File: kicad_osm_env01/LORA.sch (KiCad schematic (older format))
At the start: 15 parts, among them U5 ERIC-LORA, U6 RAK4270

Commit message: schematics awaiting review
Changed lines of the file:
@@
 AR Path="/60880AD8/608A2EE5" Ref="#PWR048"  Part="1"
 F 0 "#PWR048" H 2400 4175 50  0001 C CNN
-F 1 "+3V3" H 2415 4498 50  0000 C CNN
+F 1 "+3V3" V 2400 4550 50  0000 C CNN
 F 2 "" H 2400 4325 50  0001 C CNN
 F 3 "" H 2400 4325 50  0001 C CNN
@@
 U 1 1 6075834F
 P 8150 3800
-F 0 "U6" H 8150 4881 50  0000 C CNN
-F 1 "RAK4270" H 8150 4790 50  0000 C CNN
+F 0 "U6" H 8650 4775 50  0000 C CNN
+F 1 "RAK4270" H 8775 4675 50  0000 C CNN
 F 2 "Devtank_PCB_lib:RAK4270" H 7900 4175 50  0001 C CNN
 F 3 "" H 7900 4175 50  0001 C CNN

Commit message: rough layout with throwdown of parts
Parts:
- C70: footprint Capacitor_SMD:C_0603_1608Metric -> Capacitor_SMD:C_0402_1005Metric
- TP30, TP31, TP32, TP33, TP34, TP35: footprint TestPoint:TestPoint_THTPad_D1.0mm_Drill0.5mm -> TestPoint:TestPoint_Pad_D1.5mm
- U6: footprint Devtank_PCB_lib:RAK4270 -> Devtank_PCB_lib:RAK4270_WisDuo_LPWAN_Module
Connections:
- net LORA_RX: now also U6.1 (UART2_RX); no longer U6.5 (UART1_RX)
- net LORA_TX: now also U6.2 (UART2_TX); no longer U6.4 (UART1_TX)
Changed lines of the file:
@@
 $Descr A4 11693 8268
 encoding utf-8
-Sheet 3 11
+Sheet 3 9
 Title ""
 Date ""
@@
 F 0 "TP31" V 2950 3700 50  0000 C CNN
 F 1 "Test_Point" V 2950 3800 50  0001 C CNN
-F 2 "TestPoint:TestPoint_THTPad_D1.0mm_Drill0.5mm" H 3150 3425 50  0001 C CNN
+F 2 "TestPoint:TestPoint_Pad_D1.5mm" H 3150 3425 50  0001 C CNN
 F 3 "~" H 3150 3425 50  0001 C CNN
 	1    2950 3425
@@
 F 0 "TP32" V 2950 3925 50  0000 C CNN
 F 1 "Test_Point" V 2950 4025 50  0001 C CNN
-F 2 "TestPoint:TestPoint_THTPad_D1.0mm_Drill0.5mm" H 3150 3650 50  0001 C CNN
+F 2 "TestPoint:TestPoint_Pad_D1.5mm" H 3150 3650 50  0001 C CNN
 F 3 "~" H 3150 3650 50  0001 C CNN
 	1    2950 3650
@@
 F 0 "TP33" V 2950 4125 50  0000 C CNN
 F 1 "Test_Point" V 2950 4225 50  0001 C CNN
-F 2 "TestPoint:TestPoint_THTPad_D1.0mm_Drill0.5mm" H 3150 3850 50  0001 C CNN
+F 2 "TestPoint:TestPoint_Pad_D1.5mm" H 3150 3850 50  0001 C CNN
 F 3 "~" H 3150 3850 50  0001 C CNN
 	1    2950 3850
@@
 F 0 "TP30" V 2950 3475 50  0000 C CNN
 F 1 "Test_Point" V 2950 3575 50  0001 C CNN
-F 2 "TestPoint:TestPoint_THTPad_D1.0mm_Drill0.5mm" H 3150 3200 50  0001 C CNN
+F 2 "TestPoint:TestPoint_Pad_D1.5mm" H 3150 3200 50  0001 C CNN
 F 3 "~" H 3150 3200 50  0001 C CNN
 	1    2950 3200
@@
 F 0 "TP34" V 2950 4350 50  0000 C CNN
 F 1 "Test_Point" V 2950 4450 50  0001 C CNN
-F 2 "TestPoint:TestPoint_THTPad_D1.0mm_Drill0.5mm" H 3150 4075 50  0001 C CNN
+F 2 "TestPoint:TestPoint_Pad_D1.5mm" H 3150 4075 50  0001 C CNN
 F 3 "~" H 3150 4075 50  0001 C CNN
 	1    2950 4075
@@
 NoConn ~ 7275 4050
 NoConn ~ 7275 3925
-NoConn ~ 7275 3425
-NoConn ~ 7275 3300
-Wire Wire Line
-	7275 3675 6900 3675
-Wire Wire Line
-	7275 3800 6900 3800
-Text HLabel 6900 3800 0    50   Input ~ 0
+Wire Wire Line
+	7275 3425 6900 3425
+Wire Wire Line
+	7275 3300 6900 3300
+Text HLabel 6900 3300 0    50   Input ~ 0
 LORA_RX
-Text HLabel 6900 3675 0    50   Input ~ 0
+Text HLabel 6900 3425 0    50   Input ~ 0
 LORA_TX
 Text HLabel 3175 3350 0    50   Input ~ 0
@@
 F 0 "C70" H 9690 3571 50  0000 L CNN
 F 1 "100nF" H 9690 3480 50  0000 L CNN
-F 2 "Capacitor_SMD:C_0603_1608Metric" H 9613 3375 50  0001 C CNN
+F 2 "Capacitor_SMD:C_0402_1005Metric" H 9613 3375 50  0001 C CNN
 F 3 "" H 9575 3525 50  0001 C CNN
 	1    9575 3525
@@
 F 0 "TP35" V 9900 3675 50  0000 C CNN
 F 1 "Test_Point" V 9975 3625 50  0001 C CNN
-F 2 "TestPoint:TestPoint_THTPad_D1.0mm_Drill0.5mm" H 10100 3400 50  0001 C CNN
+F 2 "TestPoint:TestPoint_Pad_D1.5mm" H 10100 3400 50  0001 C CNN
 F 3 "~" H 10100 3400 50  0001 C CNN
 	1    9900 3400
@@
 F 0 "U6" H 8650 4775 50  0000 C CNN
 F 1 "RAK4270" H 8775 4675 50  0000 C CNN
-F 2 "Devtank_PCB_lib:RAK4270" H 7900 4175 50  0001 C CNN
+F 2 "Devtank_PCB_lib:RAK4270_WisDuo_LPWAN_Module" H 7900 4175 50  0001 C CNN
 F 3 "" H 7900 4175 50  0001 C CNN
 	1    8150 3800
 	1    0    0    -1
 $EndComp
+NoConn ~ 7275 3675
+NoConn ~ 7275 3800
 $EndSCHEMATC

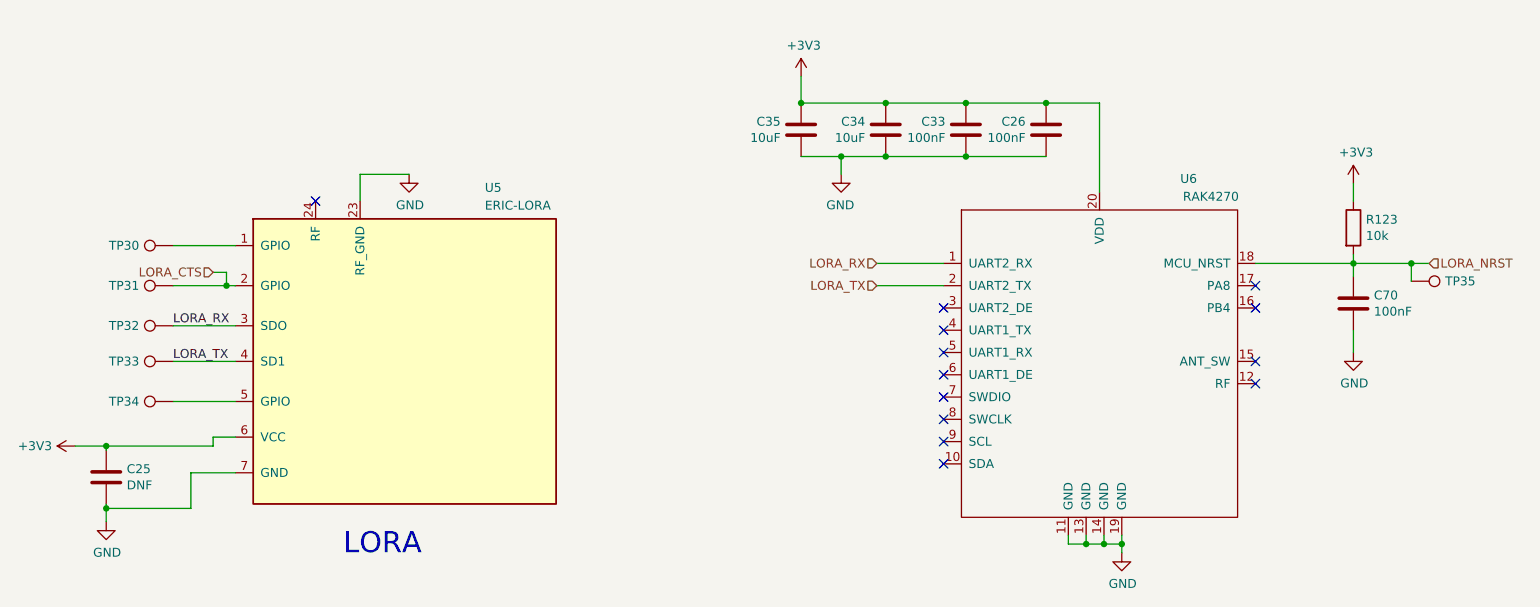
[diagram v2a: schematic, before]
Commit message: updated schematics
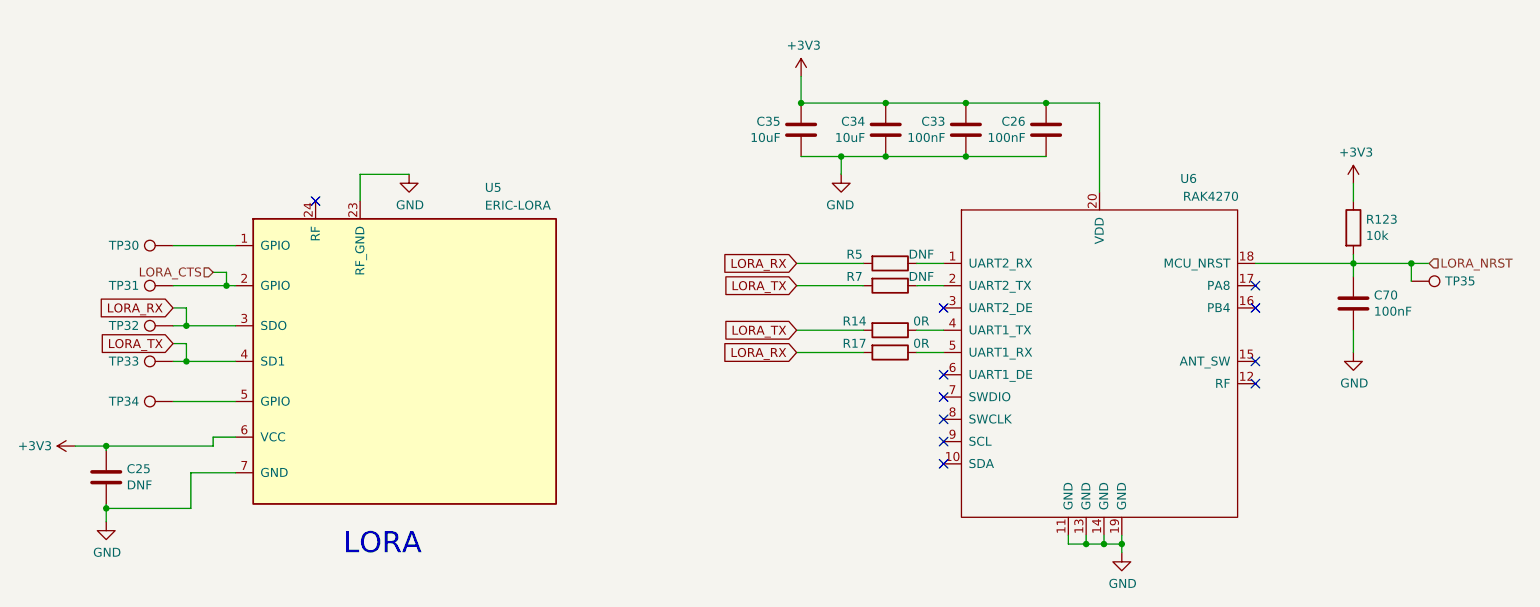
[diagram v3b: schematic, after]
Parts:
- added R14, R17: 0R, Resistor_SMD:R_0603_1608Metric, symbol device:R
- added R5, R7: DNF, Resistor_SMD:R_0603_1608Metric, symbol device:R
- C34, C35: footprint Capacitor_SMD:C_0805_2012Metric -> Capacitor_SMD:C_0402_1005Metric
- TP32, TP33: footprint TestPoint:TestPoint_Pad_D1.5mm -> TestPoint:TestPoint_THTPad_D1.0mm_Drill0.5mm
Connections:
- net LORA_RX: now also R17.2, R5.2; no longer U6.1 (UART2_RX)
- net LORA_TX: now also R14.2, R7.2; no longer U6.2 (UART2_TX)
- net at U6.4 (UART1_TX): now also R14.1
- net at U6.5 (UART1_RX): now also R17.1
- new net: R5.1, U6.1 (UART2_RX)
- new net: R7.1, U6.2 (UART2_TX)
- no-connect marks 13 -> 11
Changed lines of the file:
@@
 	3300 3425 3250 3425
 Wire Wire Line
-	3300 3650 2950 3650
-Wire Wire Line
-	3300 3850 2950 3850
-Text Label 2950 3850 0    50   ~ 0
-LORA_TX
-Text Label 2950 3650 0    50   ~ 0
-LORA_RX
+	3300 3650 3025 3650
+Wire Wire Line
+	3300 3850 3025 3850
 Wire Wire Line
 	4000 2800 4275 2800
@@
 F 0 "TP32" V 2950 3925 50  0000 C CNN
 F 1 "Test_Point" V 2950 4025 50  0001 C CNN
-F 2 "TestPoint:TestPoint_Pad_D1.5mm" H 3150 3650 50  0001 C CNN
+F 2 "TestPoint:TestPoint_THTPad_D1.0mm_Drill0.5mm" H 3150 3650 50  0001 C CNN
 F 3 "~" H 3150 3650 50  0001 C CNN
 	1    2950 3650
@@
 F 0 "TP33" V 2950 4125 50  0000 C CNN
 F 1 "Test_Point" V 2950 4225 50  0001 C CNN
-F 2 "TestPoint:TestPoint_Pad_D1.5mm" H 3150 3850 50  0001 C CNN
+F 2 "TestPoint:TestPoint_THTPad_D1.0mm_Drill0.5mm" H 3150 3850 50  0001 C CNN
 F 3 "~" H 3150 3850 50  0001 C CNN
 	1    2950 3850
@@
 F 0 "C34" H 7065 2596 50  0000 L CNN
 F 1 "10uF" H 7065 2505 50  0000 L CNN
-F 2 "Capacitor_SMD:C_0805_2012Metric" H 6988 2400 50  0001 C CNN
+F 2 "Capacitor_SMD:C_0402_1005Metric" H 6988 2400 50  0001 C CNN
 F 3 "" H 6950 2550 50  0001 C CNN
 	1    6950 2550
@@
 F 0 "C35" H 6590 2596 50  0000 L CNN
 F 1 "10uF" H 6590 2505 50  0000 L CNN
-F 2 "Capacitor_SMD:C_0805_2012Metric" H 6513 2400 50  0001 C CNN
+F 2 "Capacitor_SMD:C_0402_1005Metric" H 6513 2400 50  0001 C CNN
 F 3 "" H 6475 2550 50  0001 C CNN
 	1    6475 2550
@@
 NoConn ~ 7275 3925
 Wire Wire Line
-	7275 3425 6900 3425
-Wire Wire Line
-	7275 3300 6900 3300
-Text HLabel 6900 3300 0    50   Input ~ 0
-LORA_RX
-Text HLabel 6900 3425 0    50   Input ~ 0
-LORA_TX
+	6825 3425 6450 3425
+Wire Wire Line
+	6825 3300 6450 3300
 Text HLabel 3175 3350 0    50   Input ~ 0
 LORA_CTS
@@
 	1    0    0    -1
 $EndComp
-NoConn ~ 7275 3675
-NoConn ~ 7275 3800
+$Comp
+L device:R R5
+U 1 1 614744DC
+P 6975 3300
+F 0 "R5" V 6925 3100 50  0000 C CNN
+F 1 "DNF" V 6925 3475 50  0000 C CNN
+F 2 "Resistor_SMD:R_0603_1608Metric" V 6905 3300 50  0001 C CNN
+F 3 "" H 6975 3300 50  0001 C CNN
+	1    6975 3300
+	0    1    1    0
+$EndComp
+$Comp
+L device:R R7
+U 1 1 61475AB7
+P 6975 3425
+F 0 "R7" V 6925 3225 50  0000 C CNN
+F 1 "DNF" V 6925 3600 50  0000 C CNN
+F 2 "Resistor_SMD:R_0603_1608Metric" V 6905 3425 50  0001 C CNN
+F 3 "" H 6975 3425 50  0001 C CNN
+	1    6975 3425
+	0    1    1    0
+$EndComp
+Wire Wire Line
+	7125 3300 7275 3300
+Wire Wire Line
+	7125 3425 7275 3425
+Wire Wire Line
+	6825 3800 6450 3800
+Wire Wire Line
+	6825 3675 6450 3675
+$Comp
+L device:R R14
+U 1 1 6147C07B
+P 6975 3675
+F 0 "R14" V 6925 3475 50  0000 C CNN
+F 1 "0R" V 6925 3850 50  0000 C CNN
+F 2 "Resistor_SMD:R_0603_1608Metric" V 6905 3675 50  0001 C CNN
+F 3 "" H 6975 3675 50  0001 C CNN
+	1    6975 3675
+	0    1    1    0
+$EndComp
+$Comp
+L device:R R17
+U 1 1 6147C081
+P 6975 3800
+F 0 "R17" V 6925 3600 50  0000 C CNN
+F 1 "0R" V 6925 3975 50  0000 C CNN
+F 2 "Resistor_SMD:R_0603_1608Metric" V 6905 3800 50  0001 C CNN
+F 3 "" H 6975 3800 50  0001 C CNN
+	1    6975 3800
+	0    1    1    0
+$EndComp
+Wire Wire Line
+	7125 3675 7275 3675
+Wire Wire Line
+	7125 3800 7275 3800
+Text GLabel 6450 3300 0    50   Input ~ 0
+LORA_RX
+Text GLabel 6450 3425 0    50   Input ~ 0
+LORA_TX
+Text GLabel 6450 3675 0    50   Input ~ 0
+LORA_TX
+Text GLabel 6450 3800 0    50   Input ~ 0
+LORA_RX
+Text GLabel 2950 3750 0    50   Input ~ 0
+LORA_TX
+Text GLabel 2950 3550 0    50   Input ~ 0
+LORA_RX
+Wire Wire Line
+	2950 3550 3025 3550
+Wire Wire Line
+	3025 3550 3025 3650
+Connection ~ 3025 3650
+Wire Wire Line
+	3025 3650 2950 3650
+Wire Wire Line
+	2950 3750 3025 3750
+Wire Wire Line
+	3025 3750 3025 3850
+Connection ~ 3025 3850
+Wire Wire Line
+	3025 3850 2950 3850
 $EndSCHEMATC

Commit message: updated schematics
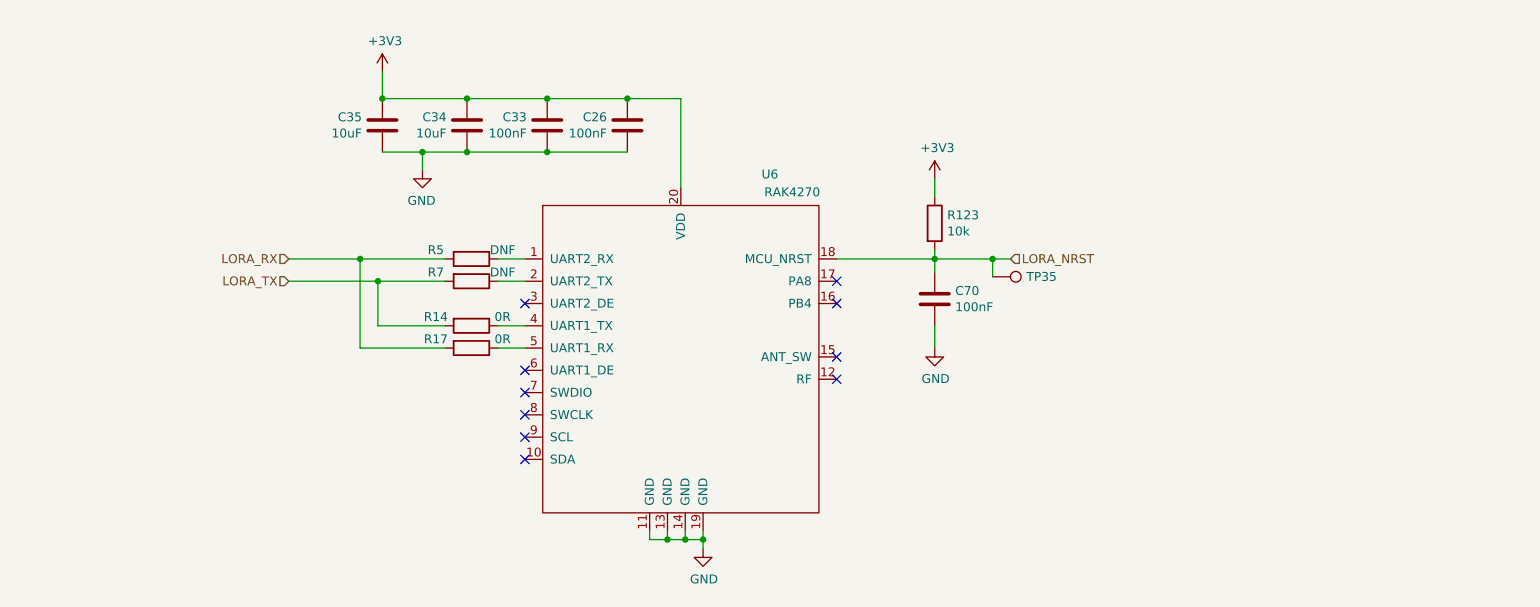
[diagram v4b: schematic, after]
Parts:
- removed C25: DNF, Capacitor_SMD:C_0402_1005Metric, symbol OSM_env01-rescue:C-device-ESP32-EVB_Rev_D-rescue
- removed TP30, TP31, TP34: Test_Point, TestPoint:TestPoint_Pad_D1.5mm, symbol OSM_env01-rescue:Test_Point-Connector-ESP32-EVB_Rev_D-rescue
- removed TP32, TP33: Test_Point, TestPoint:TestPoint_THTPad_D1.0mm_Drill0.5mm, symbol OSM_env01-rescue:Test_Point-Connector-ESP32-EVB_Rev_D-rescue
- removed U5: ERIC-LORA, Devtank_PCB_lib:eRIC-LoRa_RF_Module, symbol OSM_env01-rescue:ERIC-LORA-Devtank-ESP32-EVB_Rev_D-rescue
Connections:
- no-connect marks 11 -> 10
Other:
- note removed: "LORA"
- moved on the sheet: C26, C33, C34, C35, C70, R123, R14, R17, R5, R7, TP35, U6

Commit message: Updated schematics
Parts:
- added L4: 2A/0.05DCR, Inductor_SMD:L_0402_1005Metric, symbol device:Ferrite_Bead
- added TP24, TP30: Test_Point, TestPoint:TestPoint_Pad_D1.5mm, symbol OSM_env01-rescue:Test_Point-Connector-ESP32-EVB_Rev_D-rescue
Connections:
- net +3V3: now also L4.2; no longer C26.1, C33.1, C34.1, C35.1, U6.20 (VDD)
- net at U6.3 (UART2_DE): now also TP24.1
- net at U6.6 (UART1_DE): now also TP30.1
- net LORA_NRST: no longer names the net of C70.1, R123.2, TP35.1, U6.18 (MCU_NRST)
- new net: C26.1, C33.1, C34.1, C35.1, L4.1, U6.20 (VDD)
- no-connect marks 10 -> 8
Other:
- moved on the sheet: TP35
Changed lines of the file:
@@
 encoding utf-8
 Sheet 3 9
-Title ""
-Date ""
-Rev ""
-Comp ""
+Title "Open Smart Monitor"
+Date "2021-09-22"
+Rev "B"
+Comp "Devtank LTD"
 Comment1 ""
 Comment2 ""
@@
 Connection ~ 4600 2375
 Wire Wire Line
-	4600 2375 4125 2375
-Wire Wire Line
 	5500 2675 5050 2675
 Connection ~ 5050 2675
@@
 Wire Wire Line
 	5725 4850 5825 4850
-$Comp
-L power:+3V3 #PWR?
-U 1 1 608CFA4E
-P 4125 2225
-AR Path="/608CFA4E" Ref="#PWR?"  Part="1"
-AR Path="/60880AD8/608CFA4E" Ref="#PWR053"  Part="1"
-F 0 "#PWR053" H 4125 2075 50  0001 C CNN
-F 1 "+3V3" H 4140 2398 50  0000 C CNN
-F 2 "" H 4125 2225 50  0001 C CNN
-F 3 "" H 4125 2225 50  0001 C CNN
-	1    4125 2225
-	1    0    0    -1
-$EndComp
-Wire Wire Line
-	4125 2375 4125 2225
-Connection ~ 4125 2375
 NoConn ~ 6675 3950
 NoConn ~ 6675 3825
 NoConn ~ 6675 3525
 NoConn ~ 6675 3400
-NoConn ~ 4925 3525
 NoConn ~ 4925 4400
 NoConn ~ 4925 4275
 NoConn ~ 4925 4150
 NoConn ~ 4925 4025
-NoConn ~ 4925 3900
 Wire Wire Line
 	4475 3400 4100 3400
-Text HLabel 7650 3275 2    50   Input ~ 0
-LORA_NRST
 $Comp
 L device:R R123
@@
 Wire Wire Line
 	7225 3275 7550 3275
-Wire Wire Line
-	7550 3375 7550 3275
-Connection ~ 7550 3275
-Wire Wire Line
-	7550 3275 7650 3275
 $Comp
 L OSM_env01-rescue:Test_Point-Connector-ESP32-EVB_Rev_D-rescue TP?
 U 1 1 60A76064
-P 7550 3375
+P 7550 3275
 AR Path="/5F6F7717/60A76064" Ref="TP?"  Part="1"
 AR Path="/60A76064" Ref="TP?"  Part="1"
 AR Path="/608F4675/60A76064" Ref="TP?"  Part="1"
 AR Path="/60880AD8/60A76064" Ref="TP35"  Part="1"
-F 0 "TP35" V 7550 3650 50  0000 C CNN
-F 1 "Test_Point" V 7625 3600 50  0001 C CNN
-F 2 "TestPoint:TestPoint_Pad_D1.5mm" H 7750 3375 50  0001 C CNN
-F 3 "~" H 7750 3375 50  0001 C CNN
-	1    7550 3375
+F 0 "TP35" V 7550 3550 50  0000 C CNN
+F 1 "Test_Point" V 7625 3500 50  0001 C CNN
+F 2 "TestPoint:TestPoint_Pad_D1.5mm" H 7750 3275 50  0001 C CNN
+F 3 "~" H 7750 3275 50  0001 C CNN
+	1    7550 3275
 	0    1    1    0
 $EndComp
@@
 	4100 3400 3600 3400
 Connection ~ 4100 3400
+Wire Wire Line
+	4925 3525 4600 3525
+$Comp
+L OSM_env01-rescue:Test_Point-Connector-ESP32-EVB_Rev_D-rescue TP?
+U 1 1 619075D3
+P 4600 3525
+AR Path="/5F6F7717/619075D3" Ref="TP?"  Part="1"
+AR Path="/619075D3" Ref="TP?"  Part="1"
+AR Path="/608F4675/619075D3" Ref="TP?"  Part="1"
+AR Path="/60880AD8/619075D3" Ref="TP24"  Part="1"
+F 0 "TP24" V 4600 3800 50  0000 C CNN
+F 1 "Test_Point" V 4675 3750 50  0001 C CNN
+F 2 "TestPoint:TestPoint_Pad_D1.5mm" H 4800 3525 50  0001 C CNN
+F 3 "~" H 4800 3525 50  0001 C CNN
+	1    4600 3525
+	0    -1   1    0
+$EndComp
+Wire Wire Line
+	4925 3900 4600 3900
+$Comp
+L OSM_env01-rescue:Test_Point-Connector-ESP32-EVB_Rev_D-rescue TP?
+U 1 1 6190A4E8
+P 4600 3900
+AR Path="/5F6F7717/6190A4E8" Ref="TP?"  Part="1"
+AR Path="/6190A4E8" Ref="TP?"  Part="1"
+AR Path="/608F4675/6190A4E8" Ref="TP?"  Part="1"
+AR Path="/60880AD8/6190A4E8" Ref="TP30"  Part="1"
+F 0 "TP30" V 4600 4175 50  0000 C CNN
+F 1 "Test_Point" V 4675 4125 50  0001 C CNN
+F 2 "TestPoint:TestPoint_Pad_D1.5mm" H 4800 3900 50  0001 C CNN
+F 3 "~" H 4800 3900 50  0001 C CNN
+	1    4600 3900
+	0    -1   1    0
+$EndComp
+$Comp
+L power:+3V3 #PWR?
+U 1 1 61A8FFEA
+P 3250 2125
+AR Path="/6064BC1D/61A8FFEA" Ref="#PWR?"  Part="1"
+AR Path="/60880AD8/61A8FFEA" Ref="#PWR0135"  Part="1"
+F 0 "#PWR0135" H 3250 1975 50  0001 C CNN
+F 1 "+3V3" H 3265 2298 50  0000 C CNN
+F 2 "" H 3250 2125 50  0001 C CNN
+F 3 "" H 3250 2125 50  0001 C CNN
+	1    3250 2125
+	1    0    0    -1
+$EndComp
+Connection ~ 4125 2375
+Wire Wire Line
+	4125 2375 4600 2375
+$Comp
+L device:Ferrite_Bead L?
+U 1 1 61ACAEED
+P 3625 2375
+AR Path="/61ACAEED" Ref="L?"  Part="1"
+AR Path="/60917DD5/61ACAEED" Ref="L?"  Part="1"
+AR Path="/608F4675/61ACAEED" Ref="L?"  Part="1"
+AR Path="/60880AD8/61ACAEED" Ref="L4"  Part="1"
+F 0 "L4" V 3351 2375 50  0000 C CNN
+F 1 "2A/0.05DCR" V 3442 2375 50  0000 C CNN
+F 2 "Inductor_SMD:L_0402_1005Metric" V 3555 2375 50  0001 C CNN
+F 3 "" H 3625 2375 50  0001 C CNN
+	1    3625 2375
+	0    1    1    0
+$EndComp
+Wire Wire Line
+	3475 2375 3250 2375
+Wire Wire Line
+	3250 2125 3250 2375
+Wire Wire Line
+	3775 2375 4125 2375
 $EndSCHEMATC

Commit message: rough throwdown of all parts
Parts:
- C34, C35: footprint Capacitor_SMD:C_0402_1005Metric -> Capacitor_SMD:C_0603_1608Metric
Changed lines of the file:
@@
 F 0 "C34" H 4715 2571 50  0000 L CNN
 F 1 "10uF" H 4715 2480 50  0000 L CNN
-F 2 "Capacitor_SMD:C_0402_1005Metric" H 4638 2375 50  0001 C CNN
+F 2 "Capacitor_SMD:C_0603_1608Metric" H 4638 2375 50  0001 C CNN
 F 3 "" H 4600 2525 50  0001 C CNN
 	1    4600 2525
@@
 F 0 "C35" H 4240 2571 50  0000 L CNN
 F 1 "10uF" H 4240 2480 50  0000 L CNN
-F 2 "Capacitor_SMD:C_0402_1005Metric" H 4163 2375 50  0001 C CNN
+F 2 "Capacitor_SMD:C_0603_1608Metric" H 4163 2375 50  0001 C CNN
 F 3 "" H 4125 2525 50  0001 C CNN
 	1    4125 2525

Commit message: Bom and gerbers added
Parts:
- TP24, TP30, TP35: footprint TestPoint:TestPoint_Pad_D1.5mm -> TestPoint:TestPoint_THTPad_D1.0mm_Drill0.5mm
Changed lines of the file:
@@
 F 0 "TP35" V 7550 3550 50  0000 C CNN
 F 1 "Test_Point" V 7625 3500 50  0001 C CNN
-F 2 "TestPoint:TestPoint_Pad_D1.5mm" H 7750 3275 50  0001 C CNN
+F 2 "TestPoint:TestPoint_THTPad_D1.0mm_Drill0.5mm" H 7750 3275 50  0001 C CNN
 F 3 "~" H 7750 3275 50  0001 C CNN
 	1    7550 3275
@@
 F 0 "TP24" V 4600 3800 50  0000 C CNN
 F 1 "Test_Point" V 4675 3750 50  0001 C CNN
-F 2 "TestPoint:TestPoint_Pad_D1.5mm" H 4800 3525 50  0001 C CNN
+F 2 "TestPoint:TestPoint_THTPad_D1.0mm_Drill0.5mm" H 4800 3525 50  0001 C CNN
 F 3 "~" H 4800 3525 50  0001 C CNN
 	1    4600 3525
@@
 F 0 "TP30" V 4600 4175 50  0000 C CNN
 F 1 "Test_Point" V 4675 4125 50  0001 C CNN
-F 2 "TestPoint:TestPoint_Pad_D1.5mm" H 4800 3900 50  0001 C CNN
+F 2 "TestPoint:TestPoint_THTPad_D1.0mm_Drill0.5mm" H 4800 3900 50  0001 C CNN
 F 3 "~" H 4800 3900 50  0001 C CNN
 	1    4600 3900
